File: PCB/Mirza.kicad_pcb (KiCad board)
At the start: 2 copper layers, 74 x 34 mm, 99 parts, among them J1 In, J2 Out, J3 Power, Q1 BCM857BS, Q10 BCM857BS, Q11 BCM847BS, Q12 BCM847BS, Q13 2SC3324, Q14 2SA1312, Q15 2SA1312, Q16 2SA1312, Q17 2SC3324, Q18 2SC3324, Q19 BCM847BS, Q2 BCM847BS, Q20 BCM857BS, Q21 BCM857BS, Q22 BCM847BS, Q23 2SA1312, Q24 2SC3324, Q25 2SC3324, Q26 2SA1312, Q27 D45H11, Q28 D44H11, Q3 2SA1312, Q4 2SC3324, Q5 2SC3324, Q6 2SC3324, Q7 2SA1312, Q8 2SA1312, Q9 BCM857BS, U1 ADA4522-1

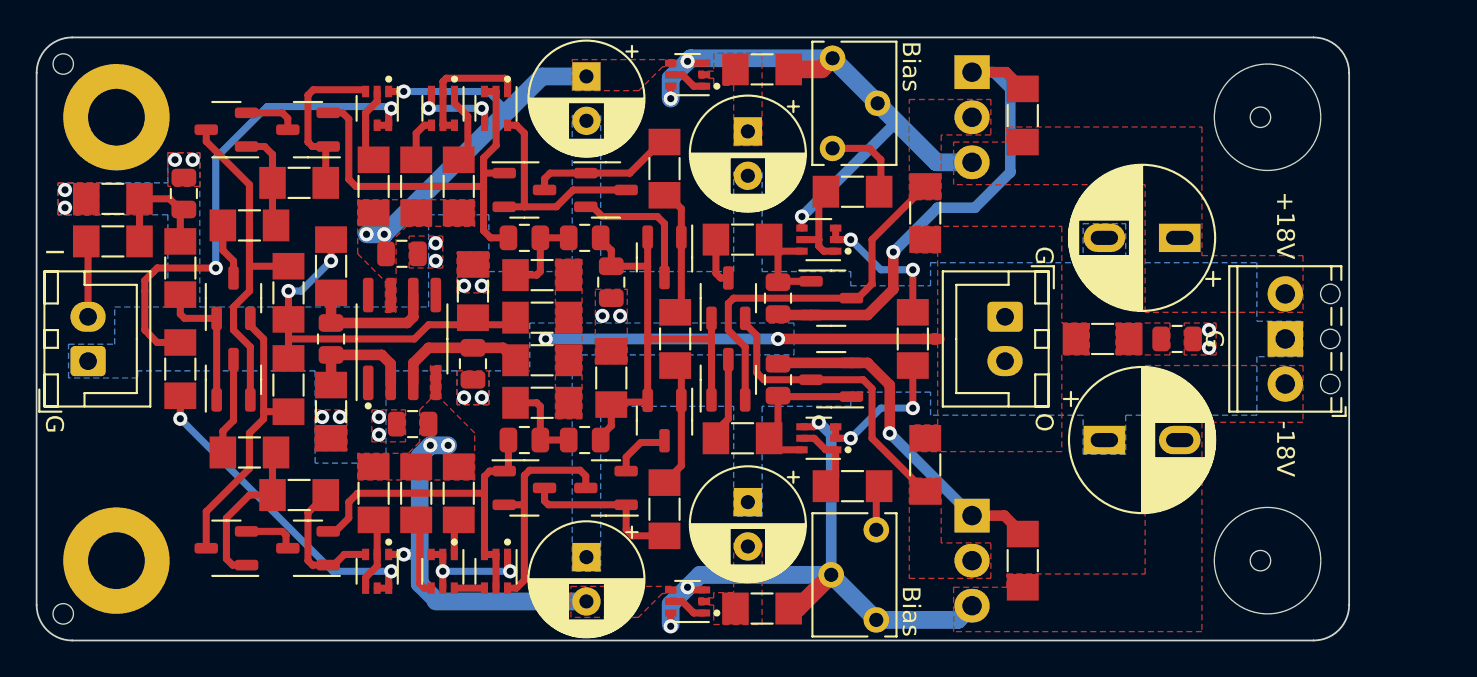
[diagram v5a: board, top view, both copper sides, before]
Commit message: 23/09/2023 update
Changed all dual transistors to BCM847DS/BCM857DS for easier soldering.
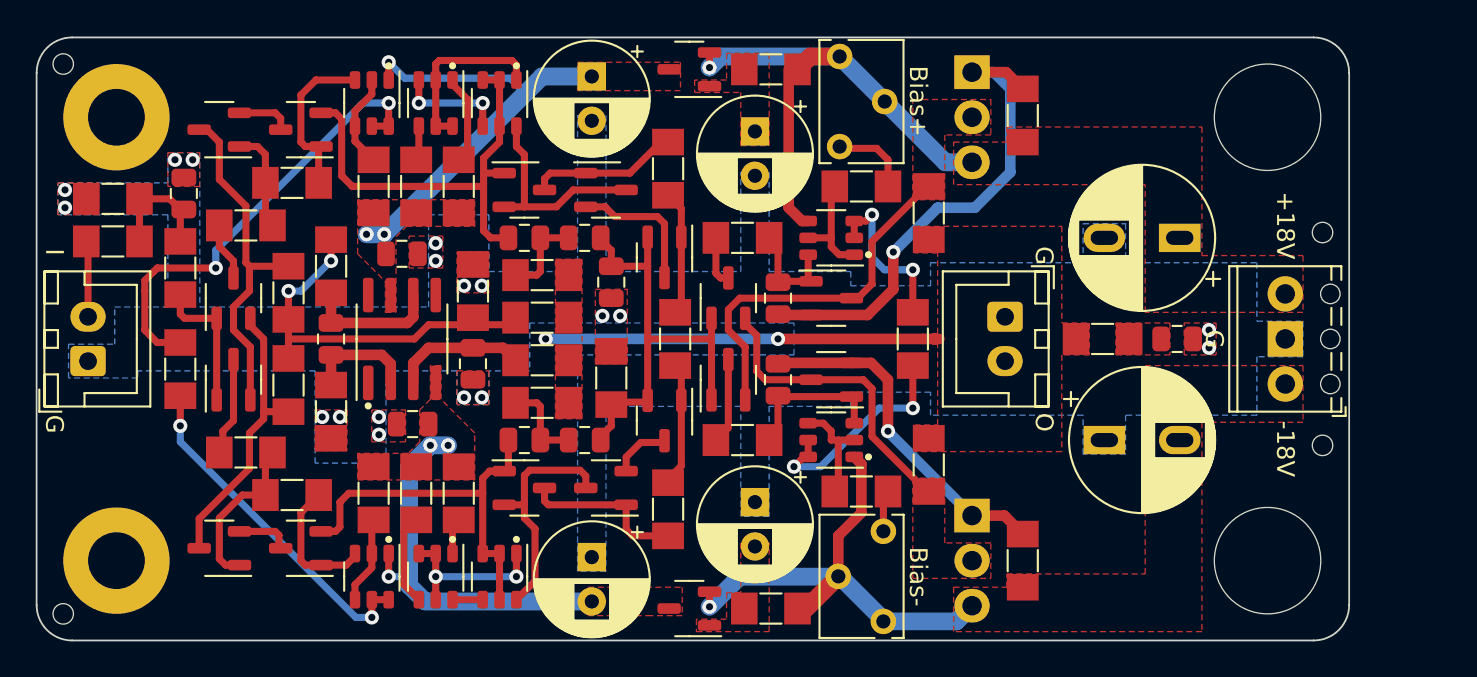
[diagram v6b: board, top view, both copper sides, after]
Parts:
- Q1, Q10, Q21, Q9: value BCM857BS -> BCM857DS; footprint Ariamelon-Package:SOT-363_SC-70-6 -> Ariamelon-Package:SOT-23-6
- Q11, Q12, Q2, Q22: value BCM847BS -> BCM847DS; footprint Ariamelon-Package:SOT-363_SC-70-6 -> Ariamelon-Package:SOT-23-6
- Q19: value BCM847BS -> 2SC3324; footprint Ariamelon-Package:SOT-363_SC-70-6 -> Ariamelon-Package:SOT-23-3
- Q20: value BCM857BS -> 2SA1312; footprint Ariamelon-Package:SOT-363_SC-70-6 -> Ariamelon-Package:SOT-23-3
- moved H5 7.38 mm to (133.0, 73.5)
- moved H6 7.38 mm to (133.0, 61.5)
- moved Q22 0.71 mm to (105.3, 73.2)
- moved Q21 0.71 mm to (105.3, 61.8)
- moved R26 0.58 mm to (107.0, 58.9)
- moved R29 0.58 mm to (107.0, 76.1)
- moved Q9 0.51 mm to (83.0, 54.2)
- moved R22 0.50 mm to (101.9, 52.3)
- moved R23 0.50 mm to (101.9, 82.7)
- moved Q12 0.50 mm to (83.0, 80.9)
- moved Q2 0.42 mm to (79.4, 80.9)
- moved Q1 0.42 mm to (79.4, 54.2)
- moved Q20 0.41 mm to (97.3, 82.7)
- moved RV1 0.41 mm to (105.8, 51.6)
- moved RV2 0.41 mm to (108.2, 83.4)
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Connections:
- C12 pad 2: Net-(Q22A-C1) -> Net-(Q22B-C2)
- C7 pad 2: Net-(Q20A-B1) -> Net-(Q20-B)
- C9 pad 1: Net-(Q19A-B1) -> Net-(Q19-B)
- Q19 pad 1: Net-(Q19A-E1) -> Net-(Q19-B)
- Q19 pad 2: Net-(Q19A-B1) -> +18V
- Q19 pad 3: +18V -> VCC
- Q20 pad 1: Net-(Q20A-E1) -> Net-(Q20-B)
- Q20 pad 2: Net-(Q20A-B1) -> -18V
- Q20 pad 3: -18V -> VEE
- Q22 pad 1: Net-(Q22A-E1) -> -18V
- Q22 pad 3: Net-(Q22A-B1) -> Net-(Q22B-C2)
- Q22 pad 4: -18V -> Net-(Q22A-B1)
- Q22 pad 5: Net-(Q22A-E1) -> Net-(Q22A-C1)
- Q26 pad 1: Net-(Q22A-C1) -> Net-(Q22B-C2)
- R22 pad 1: Net-(Q19A-B1) -> Net-(Q19-B)
- R23 pad 1: Net-(Q20A-B1) -> Net-(Q20-B)
- R25 pad 2: Net-(Q22A-B1) -> Net-(Q22A-C1)
- R28 pad 2: Net-(Q22A-C1) -> Net-(Q22B-C2)
- R29 pad 1: Net-(Q22A-E1) -> Net-(Q22A-B1)
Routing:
- net Net-(Q22B-C2): track 0.00 -> 7.43 mm
- net -18V: track 35.0 -> 27.8 mm, vias 3 -> 1
- net Net-(Q22A-C1): track 7.29 -> 12.2 mm, vias 0 -> 2
- net Net-(Q22A-E1): track 3.77 -> 0.00 mm
- net +18V: track 33.6 -> 30.3 mm, vias 3 -> 1
- net Net-(Q10A-E1): track 7.49 -> 10.0 mm
- net Net-(Q1A-C1): track 28.3 -> 25.8 mm
- net VCC: track 23.3 -> 25.8 mm
- net Net-(Q22A-B1): track 8.10 -> 5.92 mm, vias 2 -> 0
- net Net-(Q20A-E1): track 2.17 -> 0.00 mm
- net Net-(Q19A-E1): track 2.17 -> 0.00 mm
- net Net-(Q11A-E1): track 7.36 -> 9.40 mm
- net VEE: track 20.5 -> 22.5 mm
- net Net-(Q11A-B1): track 19.7 -> 21.7 mm
- net Net-(Q1A-B1): track 3.67 -> 5.33 mm
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- added copper zone on F.Cu, net Net-(Q19-B)
- added copper zone on F.Cu, net Net-(Q20-B)
- removed copper zone on F.Cu, net Net-(Q19A-B1)
- removed copper zone on F.Cu, net Net-(Q20A-B1)
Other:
- board text added: "Bias+"
- board text added: "Bias-"
- board text removed: "Bias"

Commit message: 24/09/2023 update
Increased thickness of power traces. Updated footprints for SOT-23-3 and SOT-23-6 footprints.
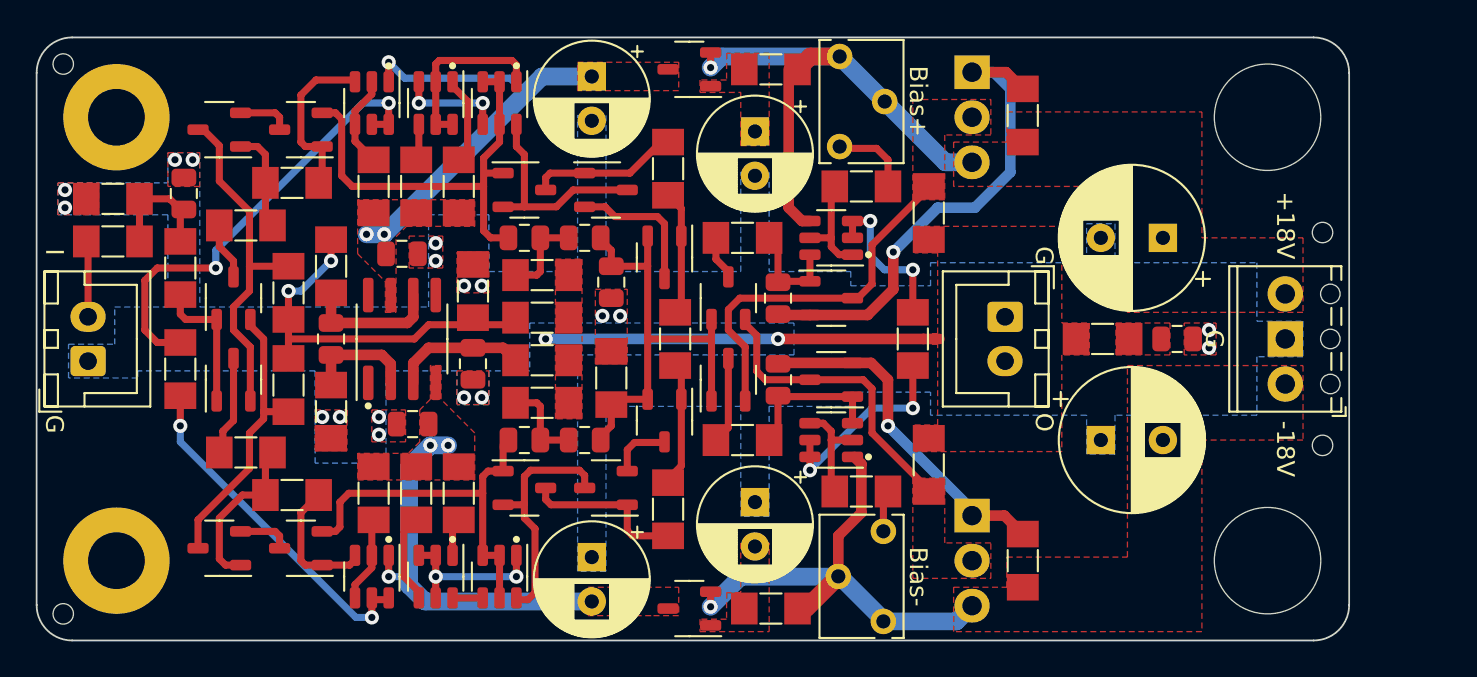
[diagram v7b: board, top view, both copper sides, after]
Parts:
- C16, C17: footprint Ariamelon-Device:CP_Radial_D8.0mm_P3.50mm_P5.00mm -> Capacitor_THT:CP_Radial_D8.0mm_P3.50mm
- moved C16 1.33 mm to (124.0, 61.8)
- moved C17 0.17 mm to (120.5, 73.2)
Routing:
- net Net-(Q22A-C1): track 12.2 -> 11.3 mm
- net Net-(Q9A-E1): track 4.81 -> 4.00 mm
- net Net-(Q11A-B1): track 21.7 -> 21.2 mm
- net Net-(Q23-E): track 2.71 -> 2.19 mm

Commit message: 28/09/2023 update
Changed size of emitter resistors to MELF0207 for better heat dissipation.
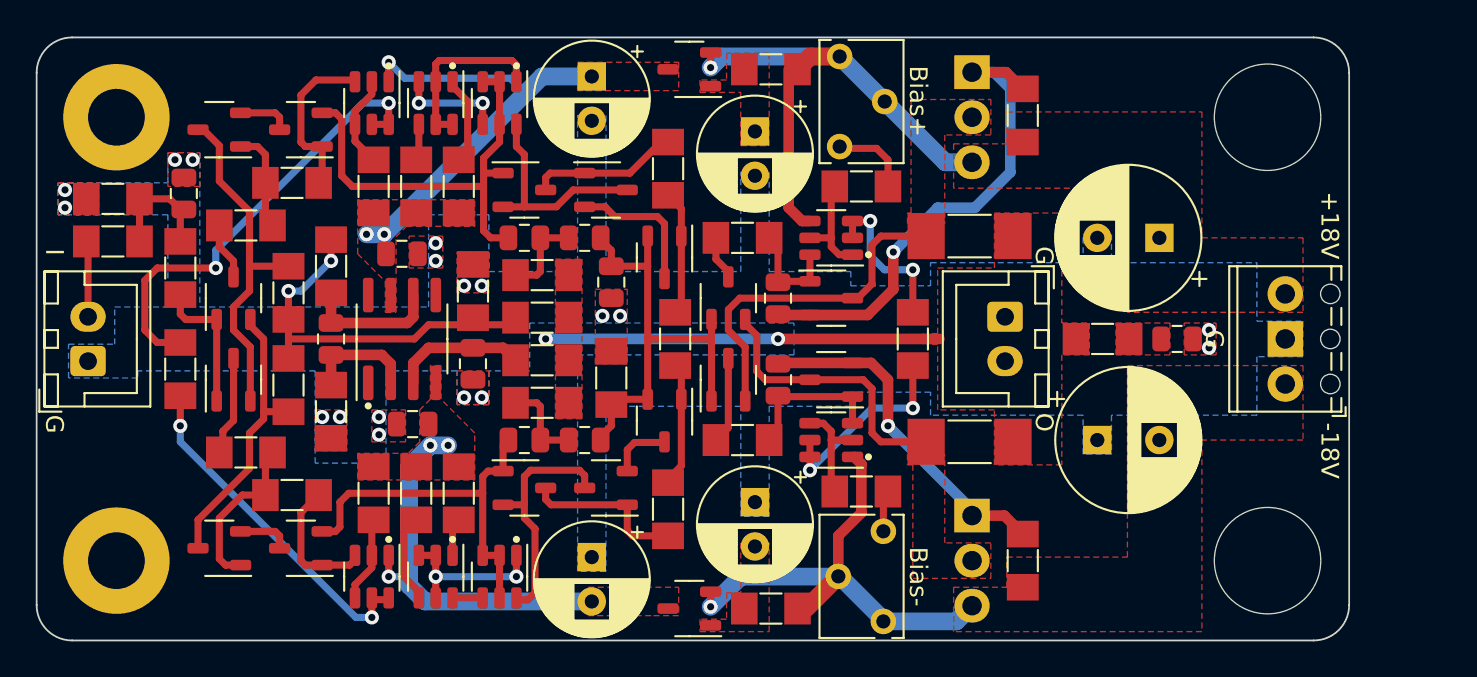
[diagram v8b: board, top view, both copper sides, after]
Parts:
- removed H3, H4, H5, H6: JLC Tooling Hole, Ariamelon-HolePad:MountingHole_JLC-Tooling
- removed R39: 1M, Resistor_SMD:R_MiniMELF_MMA-0204
- added R32: 100k, Resistor_SMD:R_MiniMELF_MMA-0204, F.Cu at (77.1, 71.6)
- C10: value 47p -> 100p
- R11, R14: value 560 -> 150
- R17, R21: value 220 -> 68
- R22, R23: value 10k -> 2k2
- R36, R37: footprint Resistor_SMD:R_MiniMELF_MMA-0204 -> Resistor_SMD:R_MELF_MMB-0207
- R7, R8: value 10 -> 68
- moved R36 2.64 mm to (113.1, 61.7), turned to 0 degrees
- moved R37 2.64 mm to (113.1, 73.3), turned to 0 degrees
- moved C16 0.20 mm to (123.8, 61.8)
- moved C17 0.20 mm to (120.3, 73.2)
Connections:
- R37 pad 1: Amp_Out -> Net-(Q23-C)
- R37 pad 2: Net-(Q23-C) -> Amp_Out
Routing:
- net Net-(Q24-C): track 20.3 -> 19.3 mm
- net Net-(Q23-C): track 16.6 -> 15.6 mm
